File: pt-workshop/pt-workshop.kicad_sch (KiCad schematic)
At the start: 2 parts, among them J101 Conn_01x10, J102 Conn_01x10

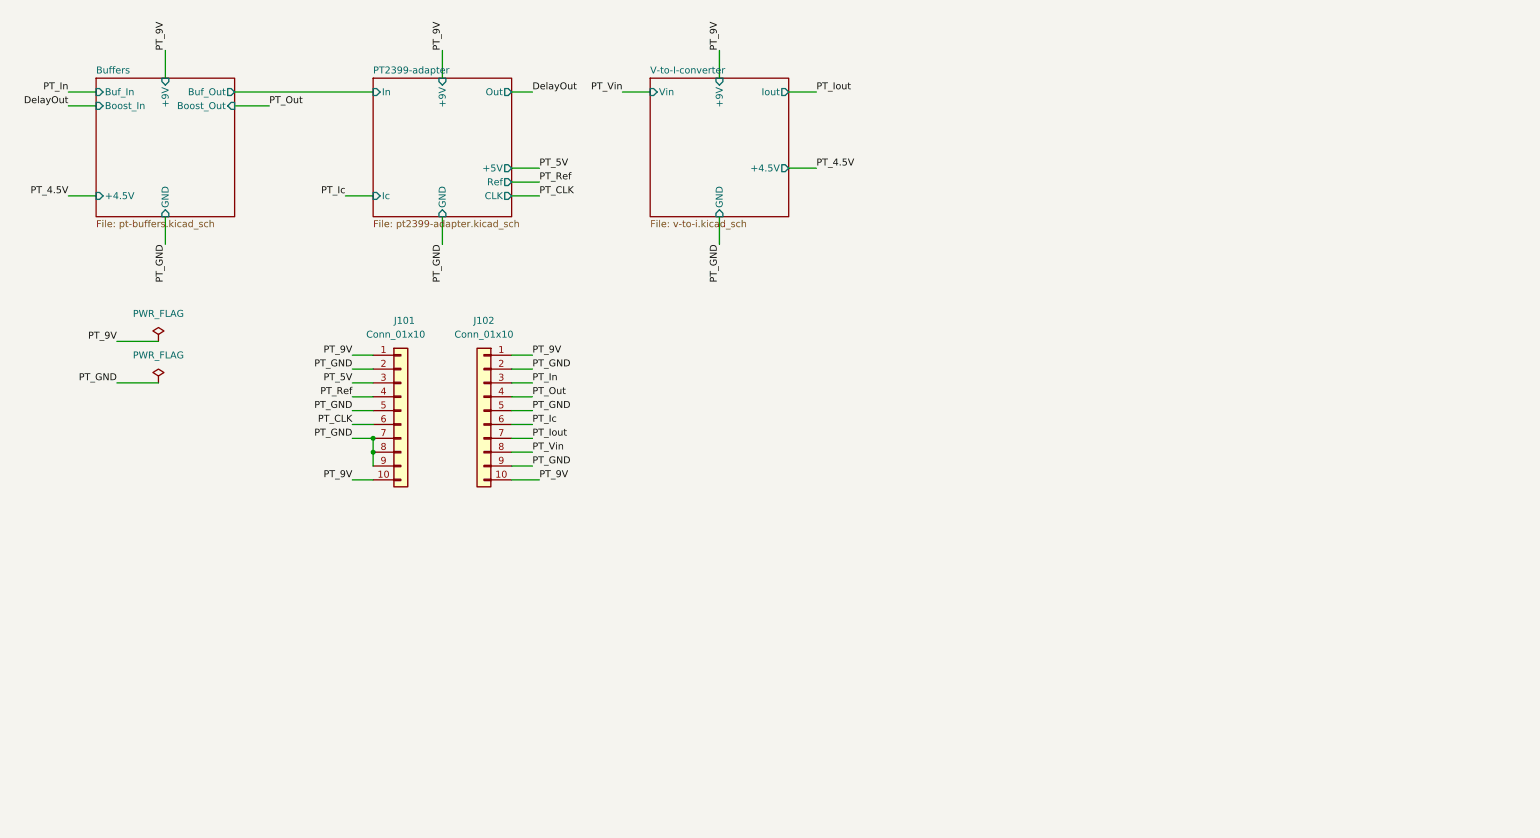
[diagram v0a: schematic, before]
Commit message: 10 pin socket
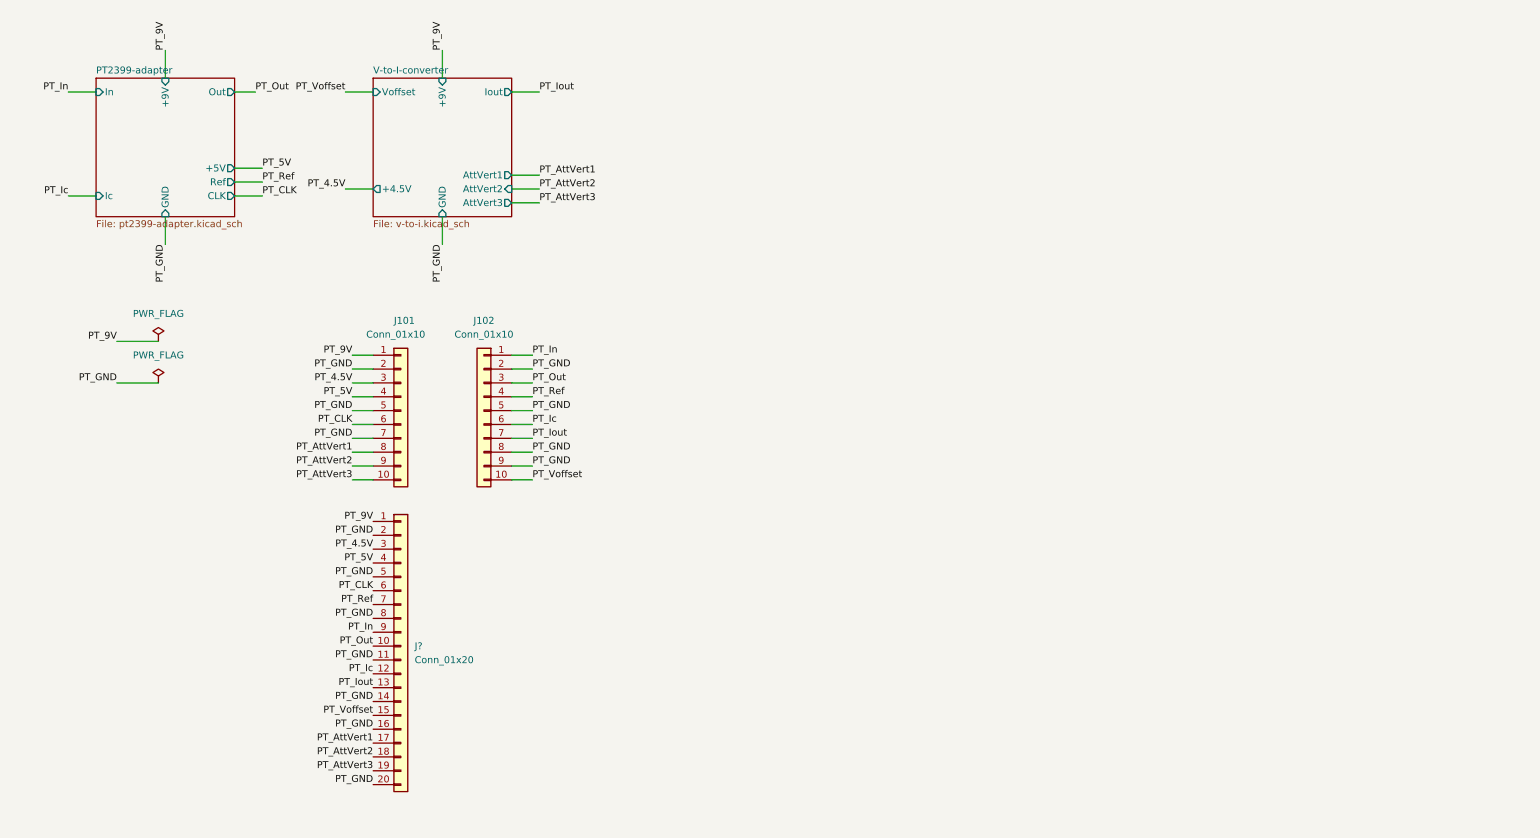
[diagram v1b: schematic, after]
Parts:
- added J?: Conn_01x20, Connector_PinSocket_2.54mm:PinSocket_1x20_P2.54mm_Vertical, symbol Connector_Generic:Conn_01x20
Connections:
- net PT_Vin is gone; now on net PT_GND: J102.8 (Pin_8)
- net PT_4.5V: now also J101.3 (Pin_3), J?.3 (Pin_3)
- net PT_5V: now also J101.4 (Pin_4), J?.4 (Pin_4); no longer J101.3 (Pin_3)
- net PT_9V: now also J?.1 (Pin_1); no longer J101.10 (Pin_10), J102.1 (Pin_1), J102.10 (Pin_10)
- net PT_CLK: now also J?.6 (Pin_6)
- net PT_GND: now also J?.11 (Pin_11), J?.14 (Pin_14), J?.16 (Pin_16), J?.2 (Pin_2), J?.20 (Pin_20), J?.5 (Pin_5), J?.8 (Pin_8); no longer J101.8 (Pin_8), J101.9 (Pin_9)
- net PT_Ic: now also J?.12 (Pin_12)
- net PT_In: now also J102.1 (Pin_1), J?.9 (Pin_9); no longer J102.3 (Pin_3)
- net PT_Iout: now also J?.13 (Pin_13)
- net PT_Out: now also J102.3 (Pin_3), J?.10 (Pin_10); no longer J102.4 (Pin_4)
- net PT_Ref: now also J102.4 (Pin_4), J?.7 (Pin_7); no longer J101.4 (Pin_4)
- new net PT_AttVert1: J101.8 (Pin_8), J?.17 (Pin_17)
- new net PT_AttVert2: J101.9 (Pin_9), J?.18 (Pin_18)
- new net PT_AttVert3: J101.10 (Pin_10), J?.19 (Pin_19)
- new net PT_Voffset: J102.10 (Pin_10), J?.15 (Pin_15)
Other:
- removed sheet Buffers
- sheet V-to-I-converter ports: added AttVert1, AttVert2, AttVert3, Voffset; removed Vin

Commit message: Board layed out
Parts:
- removed J101, J102: Conn_01x10, Connector_PinSocket_2.54mm:PinSocket_1x10_P2.54mm_Vertical, symbol Connector_Generic:Conn_01x10
- added J104: Conn_01x20, Connector_PinSocket_2.54mm:PinSocket_1x20_P2.54mm_Vertical, symbol Connector_Generic:Conn_01x20
- gave numbers to parts that had none: 1
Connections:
- net PT_4.5V: now also J104.3 (Pin_3)
- net PT_5V: now also J104.4 (Pin_4)
- net PT_9V: now also J104.1 (Pin_1)
- net PT_AttVert1: now also J104.17 (Pin_17)
- net PT_AttVert2: now also J104.18 (Pin_18)
- net PT_AttVert3: now also J104.19 (Pin_19)
- net PT_CLK: now also J104.6 (Pin_6)
- net PT_GND: now also J104.11 (Pin_11), J104.14 (Pin_14), J104.16 (Pin_16), J104.2 (Pin_2), J104.20 (Pin_20), J104.5 (Pin_5), J104.8 (Pin_8)
- net PT_Ic: now also J104.12 (Pin_12)
- net PT_In: now also J104.9 (Pin_9)
- net PT_Iout: now also J104.13 (Pin_13)
- net PT_Out: now also J104.10 (Pin_10)
- net PT_Ref: now also J104.7 (Pin_7)
- net PT_Voffset: now also J104.15 (Pin_15)
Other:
- moved on the sheet: J103

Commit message: wip
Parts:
- added H101, H103: GND, MountingHole:MountingHole_3.2mm_M3_ISO14580_Pad, symbol Mechanical:MountingHole_Pad
- added H102: 1, MountingHole:MountingHole_3.2mm_M3, symbol Mechanical:MountingHole
- added H104: 2, MountingHole:MountingHole_3.2mm_M3, symbol Mechanical:MountingHole
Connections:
- net PT_GND: now also H101.1, H103.1
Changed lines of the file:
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@@
 (kicad_sch (version 20211123) (generator eeschema)
   (paper "A4")
+  (junction (at 27.94 93.98) (diameter 0) (color 0 0 0 0)
+  )
   (wire (pts (xy 38.1 20.32) (xy 38.1 25.4))
     (stroke (width 0) (type default) (color 0 0 0 0))
@@
     (stroke (width 0) (type default) (color 0 0 0 0))
   )
+  (wire (pts (xy 27.94 93.98) (xy 27.94 97.79))
+    (stroke (width 0) (type default) (color 0 0 0 0))
+  )
   (wire (pts (xy 71.12 27.94) (xy 76.2 27.94))
     (stroke (width 0) (type default) (color 0 0 0 0))
@@
     (stroke (width 0) (type default) (color 0 0 0 0))
   )
+  (wire (pts (xy 27.94 93.98) (xy 38.1 93.98))
+    (stroke (width 0) (type default) (color 0 0 0 0))
+  )
   (wire (pts (xy 29.21 81.28) (xy 36.83 81.28))
     (stroke (width 0) (type default) (color 0 0 0 0))
@@
     (effects (font (size 1.27 1.27)) (justify left bottom))
   )
+  (label "PT_GND" (at 27.94 97.79 270)
+    (effects (font (size 1.27 1.27)) (justify right bottom))
+  )
   (label "PT_4.5V" (at 101.6 118.11 0)
     (effects (font (size 1.27 1.27)) (justify left bottom))
@@
   (label "PT_GND" (at 29.21 81.28 180)
     (effects (font (size 1.27 1.27)) (justify right bottom))
+  )
+  (symbol (lib_id "Mechanical:MountingHole") (at 27.94 111.76 0) (unit 1)
+    (in_bom yes) (on_board yes) (fields_autoplaced)
+    (property "Reference" "H102" (id 0) (at 30.48 110.4899 0)
+      (effects (font (size 1.27 1.27)) (justify left))
+    )
+    (property "Value" "1" (id 1) (at 30.48 113.0299 0)
+      (effects (font (size 1.27 1.27)) (justify left))
+    )
+    (property "Footprint" "MountingHole:MountingHole_3.2mm_M3" (id 2) (at 27.94 111.76 0)
+      (effects (font (size 1.27 1.27)) hide)
+    )
+    (property "Datasheet" "~" (id 3) (at 27.94 111.76 0)
+      (effects (font (size 1.27 1.27)) hide)
+    )
+  )
+  (symbol (lib_id "Mechanical:MountingHole_Pad") (at 38.1 91.44 0) (unit 1)
+    (in_bom yes) (on_board yes) (fields_autoplaced)
+    (property "Reference" "H103" (id 0) (at 40.64 88.8999 0)
+      (effects (font (size 1.27 1.27)) (justify left))
+    )
+    (property "Value" "GND" (id 1) (at 40.64 91.4399 0)
+      (effects (font (size 1.27 1.27)) (justify left))
+    )
+    (property "Footprint" "MountingHole:MountingHole_3.2mm_M3_ISO14580_Pad" (id 2) (at 38.1 91.44 0)
+      (effects (font (size 1.27 1.27)) hide)
+    )
+    (property "Datasheet" "~" (id 3) (at 38.1 91.44 0)
+      (effects (font (size 1.27 1.27)) hide)
+    )
+    (pin "1")
   )
   (symbol (lib_id "power:PWR_FLAG") (at 36.83 81.28 0) (unit 1)
@@
     )
     (pin "1")
+  )
+  (symbol (lib_id "Mechanical:MountingHole") (at 38.1 111.76 0) (unit 1)
+    (in_bom yes) (on_board yes) (fields_autoplaced)
+    (property "Reference" "H104" (id 0) (at 40.64 110.4899 0)
+      (effects (font (size 1.27 1.27)) (justify left))
+    )
+    (property "Value" "2" (id 1) (at 40.64 113.0299 0)
+      (effects (font (size 1.27 1.27)) (justify left))
+    )
+    (property "Footprint" "MountingHole:MountingHole_3.2mm_M3" (id 2) (at 38.1 111.76 0)
+      (effects (font (size 1.27 1.27)) hide)
+    )
+    (property "Datasheet" "~" (id 3) (at 38.1 111.76 0)
+      (effects (font (size 1.27 1.27)) hide)
+    )
   )
   (symbol (lib_id "power:PWR_FLAG") (at 36.83 73.66 0) (unit 1)
@@
     (pin "9")
   )
+  (symbol (lib_id "Mechanical:MountingHole_Pad") (at 27.94 91.44 0) (unit 1)
+    (in_bom yes) (on_board yes) (fields_autoplaced)
+    (property "Reference" "H101" (id 0) (at 30.48 88.8999 0)
+      (effects (font (size 1.27 1.27)) (justify left))
+    )
+    (property "Value" "GND" (id 1) (at 30.48 91.4399 0)
+      (effects (font (size 1.27 1.27)) (justify left))
+    )
+    (property "Footprint" "MountingHole:MountingHole_3.2mm_M3_ISO14580_Pad" (id 2) (at 27.94 91.44 0)
+      (effects (font (size 1.27 1.27)) hide)
+    )
+    (property "Datasheet" "~" (id 3) (at 27.94 91.44 0)
+      (effects (font (size 1.27 1.27)) hide)
+    )
+    (pin "1")
+  )
   (sheet (at 76.2 25.4) (size 25.4 25.4) (fields_autoplaced)
     (stroke (width 0.1524) (type solid) (color 0 0 0 0))
@@
       (reference "C303") (unit 1) (value "100n") (footprint "Capacitor_SMD:C_0603_1608Metric_Pad1.08x0.95mm_HandSolder")
     )
+    (path "/a7268b3c-a341-446a-9b98-a2775b406e83"
+      (reference "H101") (unit 1) (value "GND") (footprint "MountingHole:MountingHole_3.2mm_M3_ISO14580_Pad")
+    )
+    (path "/10d7c6c2-4f59-4038-8184-3c07bcc41c87"
+      (reference "H102") (unit 1) (value "1") (footprint "MountingHole:MountingHole_3.2mm_M3")
+    )
+    (path "/198e2226-085a-4324-a26f-2dda12d66fb1"
+      (reference "H103") (unit 1) (value "GND") (footprint "MountingHole:MountingHole_3.2mm_M3_ISO14580_Pad")
+    )
+    (path "/365666dd-410c-44a8-9529-c2088a0c235e"
+      (reference "H104") (unit 1) (value "2") (footprint "MountingHole:MountingHole_3.2mm_M3")
+    )
     (path "/64611dd7-8239-43b9-a43d-68bf1df7210f"

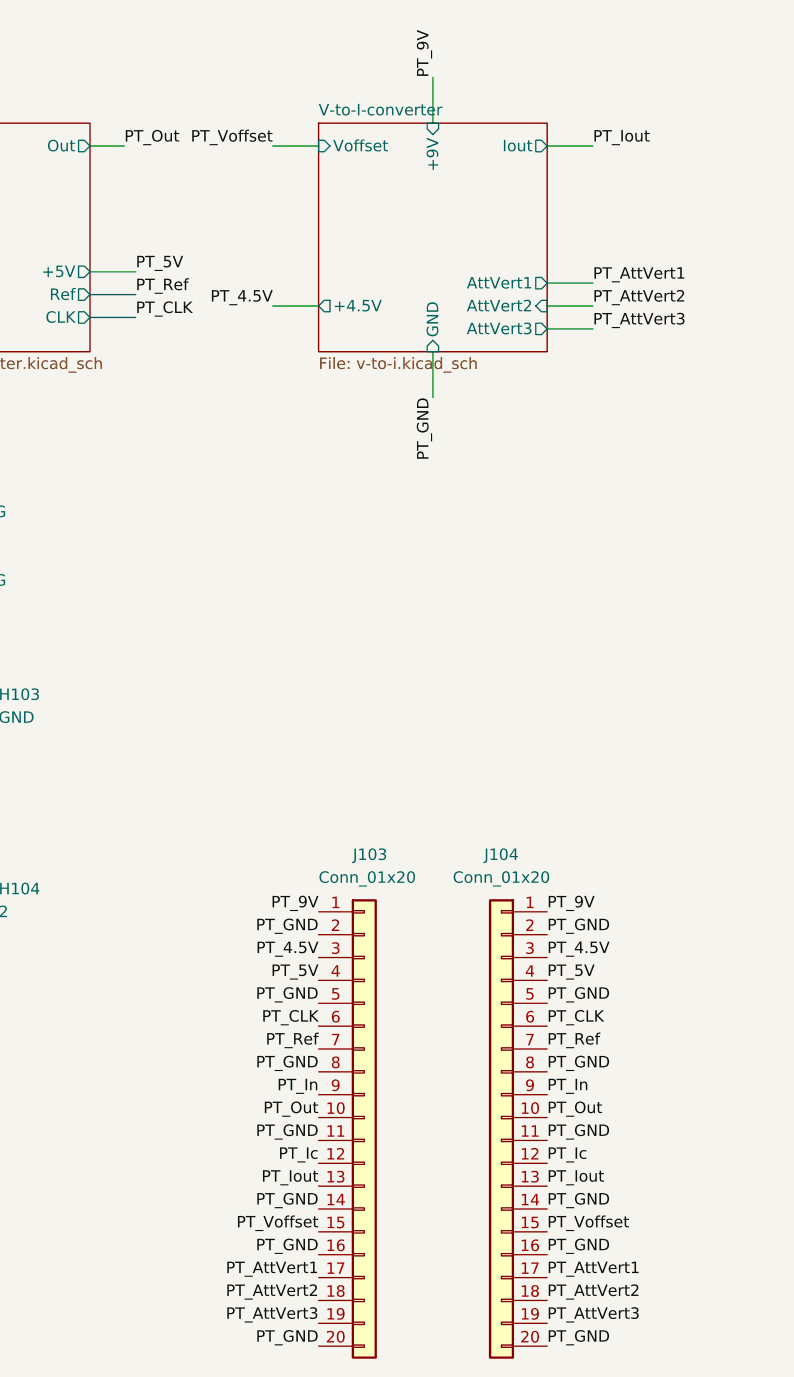
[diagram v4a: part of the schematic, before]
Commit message: PTT without attverts
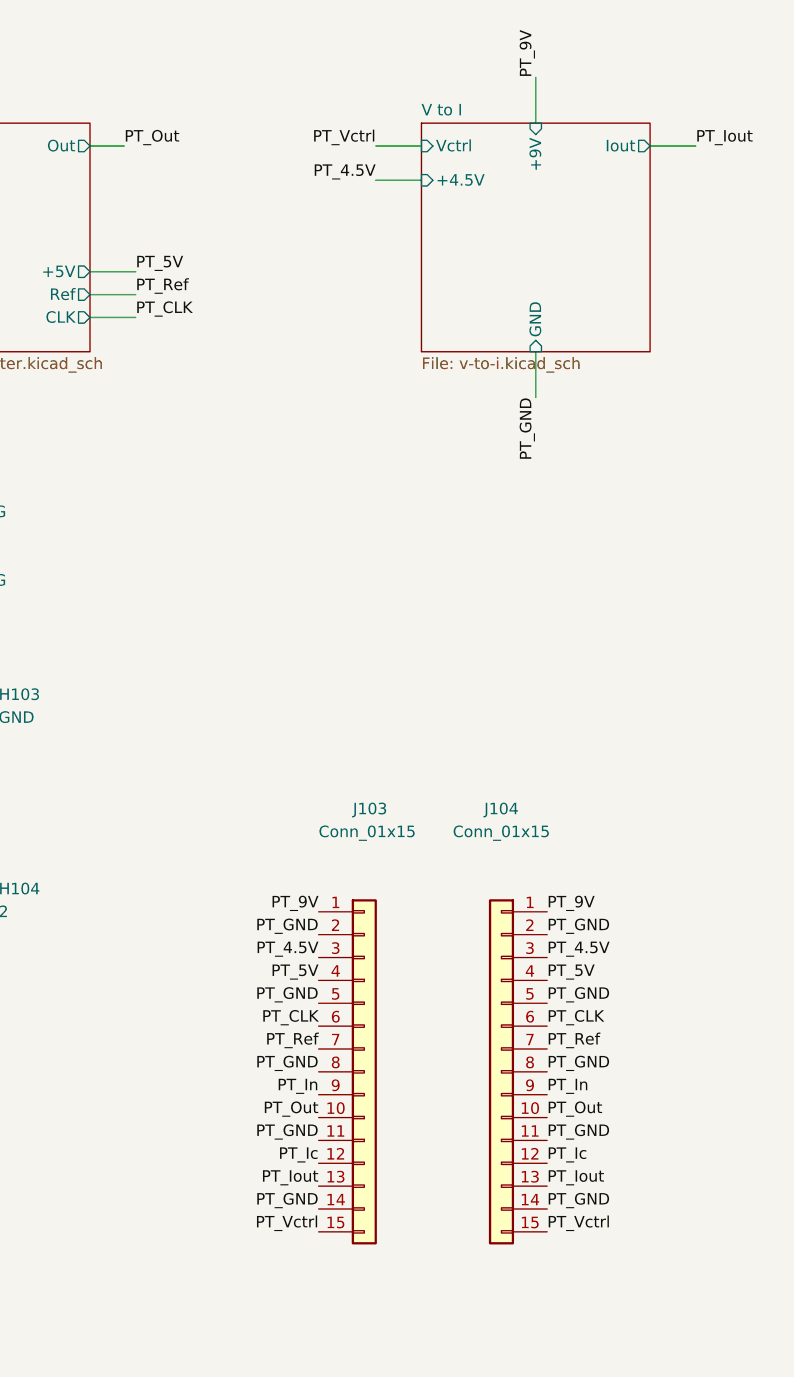
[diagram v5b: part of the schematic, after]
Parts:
- J103, J104: value Conn_01x20 -> Conn_01x15; footprint Connector_PinSocket_2.54mm:PinSocket_1x20_P2.54mm_Vertical -> Connector_PinSocket_2.54mm:PinSocket_1x15_P2.54mm_Vertical; symbol Connector_Generic:Conn_01x20 -> Connector_Generic:Conn_01x15
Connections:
- net PT_GND: no longer J103.16 (Pin_16), J103.20 (Pin_20), J104.16 (Pin_16), J104.20 (Pin_20)
- removed net PT_AttVert1: J103.17 (Pin_17), J104.17 (Pin_17)
- removed net PT_AttVert2: J103.18 (Pin_18), J104.18 (Pin_18)
- removed net PT_AttVert3: J103.19 (Pin_19), J104.19 (Pin_19)
- net PT_Voffset renamed PT_Vctrl
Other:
- sheet V-to-I-converter renamed V to I
- sheet V to I ports: added Vctrl; removed AttVert1, AttVert2, AttVert3, Voffset

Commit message: PTT schem export
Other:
- company: (none) -> Pedal Markt
- title: (none) -> PTT
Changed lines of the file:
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@@
 (kicad_sch (version 20211123) (generator eeschema)
   (paper "A4")
+  (title_block
+    (title "PTT")
+    (date "2024-05-11")
+    (rev "v1rev2")
+    (company "Pedal Markt")
+    (comment 1 "Andrey Salomatin")
+  )
   (junction (at 27.94 93.98) (diameter 0) (color 0 0 0 0)
   )

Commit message: Add TODOs
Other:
- note added: "Add latch-up protection circuit"
- note added: "TODO:"
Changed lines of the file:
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@@
     (stroke (width 0) (type default) (color 0 0 0 0))
+  )
+  (text "TODO:" (at 248.92 19.05 0)
+    (effects (font (size 3.54 3.54)) (justify left bottom))
+  )
+  (text "Add latch-up protection circuit\n" (at 250.19 22.86 0)
+    (effects (font (size 1.27 1.27)) (justify left bottom))
   )
   (label "PT_Vctrl" (at 76.2 148.59 180)
